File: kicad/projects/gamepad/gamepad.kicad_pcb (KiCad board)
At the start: 2 copper layers, 203.2 x 97.8 mm, 71 parts, among them J1 peripheral_addr_bus_connector, J10 Pad 2 SNES, J11 Conn_01x03_Pin, J2 peripheral_aux_connector, J3 peripheral_membank_connector, J4 PAD 1 ACTIVE, J5 PAD 2 ACTIVE, J6 Conn_02x05_Odd_Even, J7 Pad 1 header, J8 Pad 1 SNES, J9 Pad 2 header, U1 74HC161, U10 74HC245, U11 74HC245, U12 74HC245, U13 74HC245, U14 74HC00, U2 74HC161, U3 74HC595, U4 74HC595, U5 74HC595, U6 74HC595, U7 74HC14, U8 74HC00, U9 74HC161

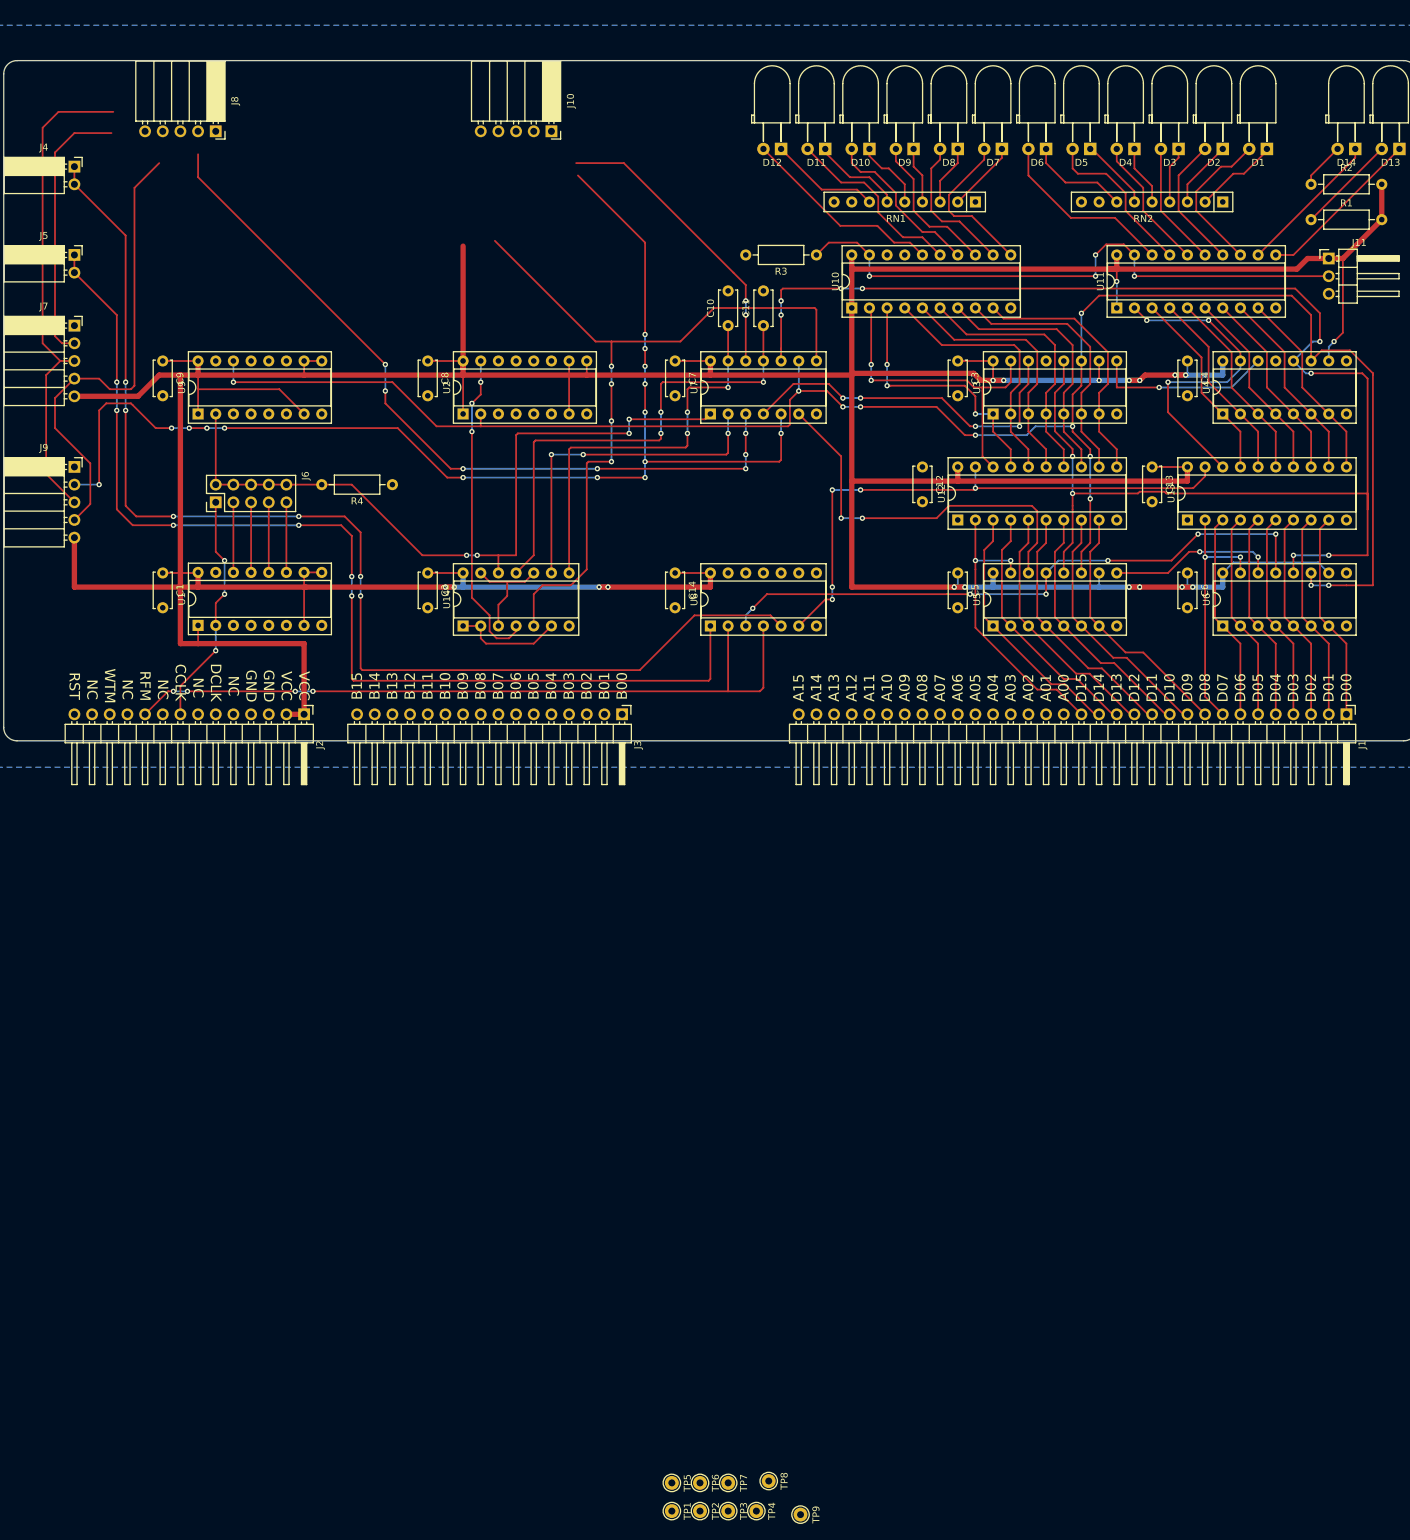
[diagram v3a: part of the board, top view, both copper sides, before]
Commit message: Add gamepad connector and almost complete on gamepad PCB
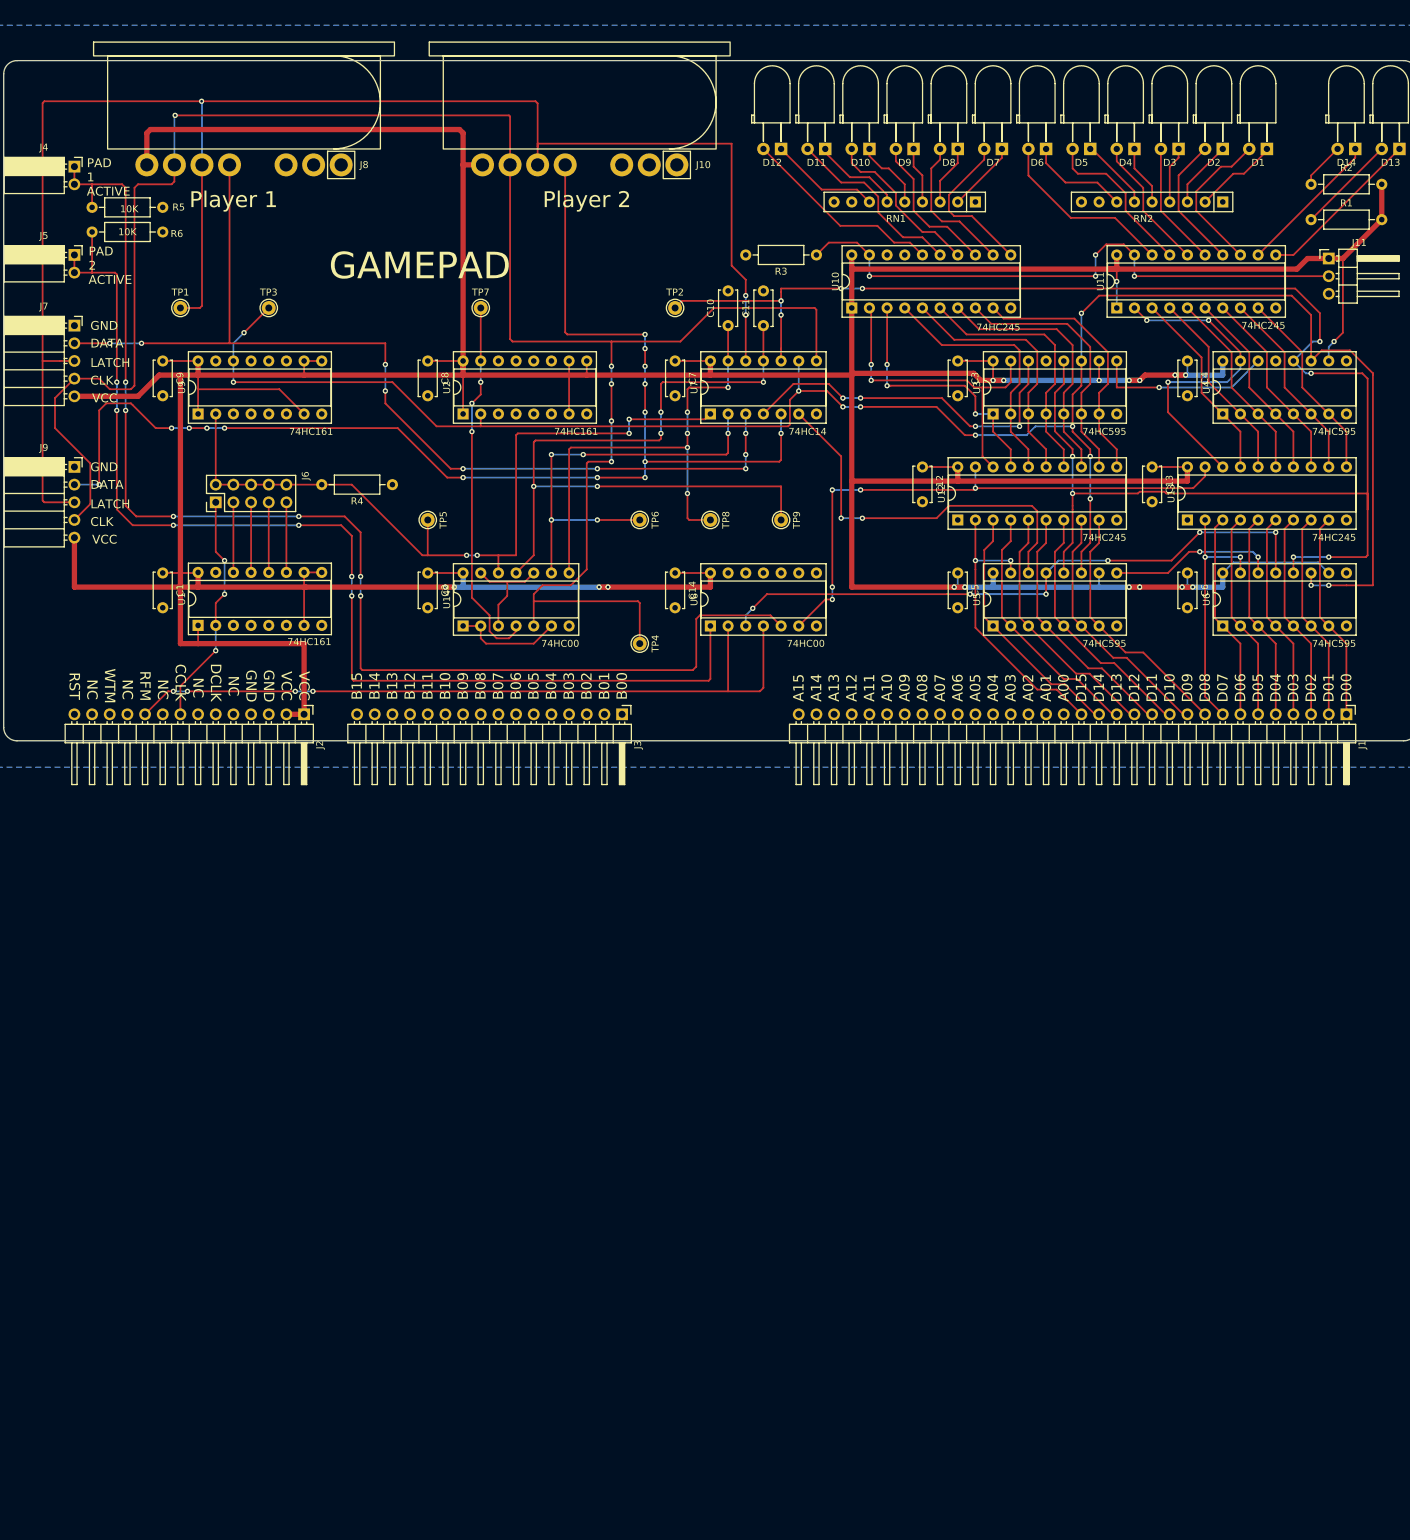
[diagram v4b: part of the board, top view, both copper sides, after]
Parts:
- added R5: 10K, Resistor_THT:R_Axial_DIN0207_L6.3mm_D2.5mm_P10.16mm_Horizontal, F.Cu at (63.5, 71.9)
- added R6: 10K, Resistor_THT:R_Axial_DIN0207_L6.3mm_D2.5mm_P10.16mm_Horizontal, F.Cu at (63.5, 75.4)
- J10, J8: footprint Connector_PinSocket_2.54mm:PinSocket_1x05_P2.54mm_Horizontal -> sixteen-bit-computer:snes-rightangle-connector
- moved TP1 186.8 mm to (76.2, 86.4), turned to 180 degrees
- moved TP3 185.2 mm to (88.9, 86.4), turned to 180 degrees
- moved TP2 173.0 mm to (147.3, 86.4), turned to 180 degrees
- moved TP7 172.6 mm to (119.4, 86.4), turned to 180 degrees
- moved TP9 143.0 mm to (162.6, 116.8)
- moved TP5 142.8 mm to (111.8, 116.8)
- moved TP6 138.7 mm to (142.2, 116.8)
- moved TP8 138.4 mm to (152.4, 116.8)
- moved TP4 125.8 mm to (142.2, 134.6)
- moved J10 18.7 mm to (147.6, 65.8), turned to 0 degrees
- moved J8 18.7 mm to (99.3, 65.8), turned to 0 degrees
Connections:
- J10 pad 2: /PAD 2 DATA -> unconnected-(J10-Pin_2-Pad2)
- J10 pad 3: /GAMEPAD LATCH -> unconnected-(J10-Pin_3-Pad3)
- J10 pad 4: /GAMEPAD CLK -> /PAD 2 DATA
- J10 pad 5: VCC -> /GAMEPAD LATCH
- J8 pad 2: /PAD 1 DATA -> unconnected-(J8-Pin_2-Pad2)
- J8 pad 3: /GAMEPAD LATCH -> unconnected-(J8-Pin_3-Pad3)
- J8 pad 4: /GAMEPAD CLK -> /PAD 1 DATA
- J8 pad 5: VCC -> /GAMEPAD LATCH
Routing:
- net /GAMEPAD LATCH: track 113.1 -> 239.7 mm, vias 2 -> 3
- net /GAMEPAD CLK: track 179.0 -> 283.0 mm, vias 4 -> 5
- net VCC: track 769.8 -> 844.4 mm
- net Net-(C11-Pad1): track 69.4 -> 109.8 mm, vias 3 -> 5
- net /SHIFT OUT REG CLK: track 226.1 -> 241.7 mm
- net Net-(C10-Pad1): track 58.0 -> 71.7 mm, vias 3 -> 5
- net /~{BASE CLK}: track 48.1 -> 60.8 mm, vias 3 -> 5
- net /PAD 1 ACTIVE: track 171.2 -> 182.5 mm
- net /PAD 2 ACTIVE: track 154.4 -> 164.2 mm
- net /SHIFT SERIAL CLK: track 273.3 -> 283.1 mm, vias 11 -> 12
- net /PAD 2 DATA: track 171.2 -> 180.1 mm
- net Net-(U2-TC): track 45.9 -> 53.5 mm
- net /PAD 1 DATA: track 149.5 -> 142.6 mm, vias 7 -> 9
- net /BASE CLK: track 107.8 -> 112.8 mm
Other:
- board text added: "CLK"
- board text added: "DATA"
- board text added: "GAMEPAD"
- board text added: "GND"
- board text added: "LATCH"
- board text added: "PAD 1 ACTIVE"
- board text added: "PAD 2 ACTIVE"
- board text added: "Player 1"
- board text added: "Player 2"
- board text added: "VCC"

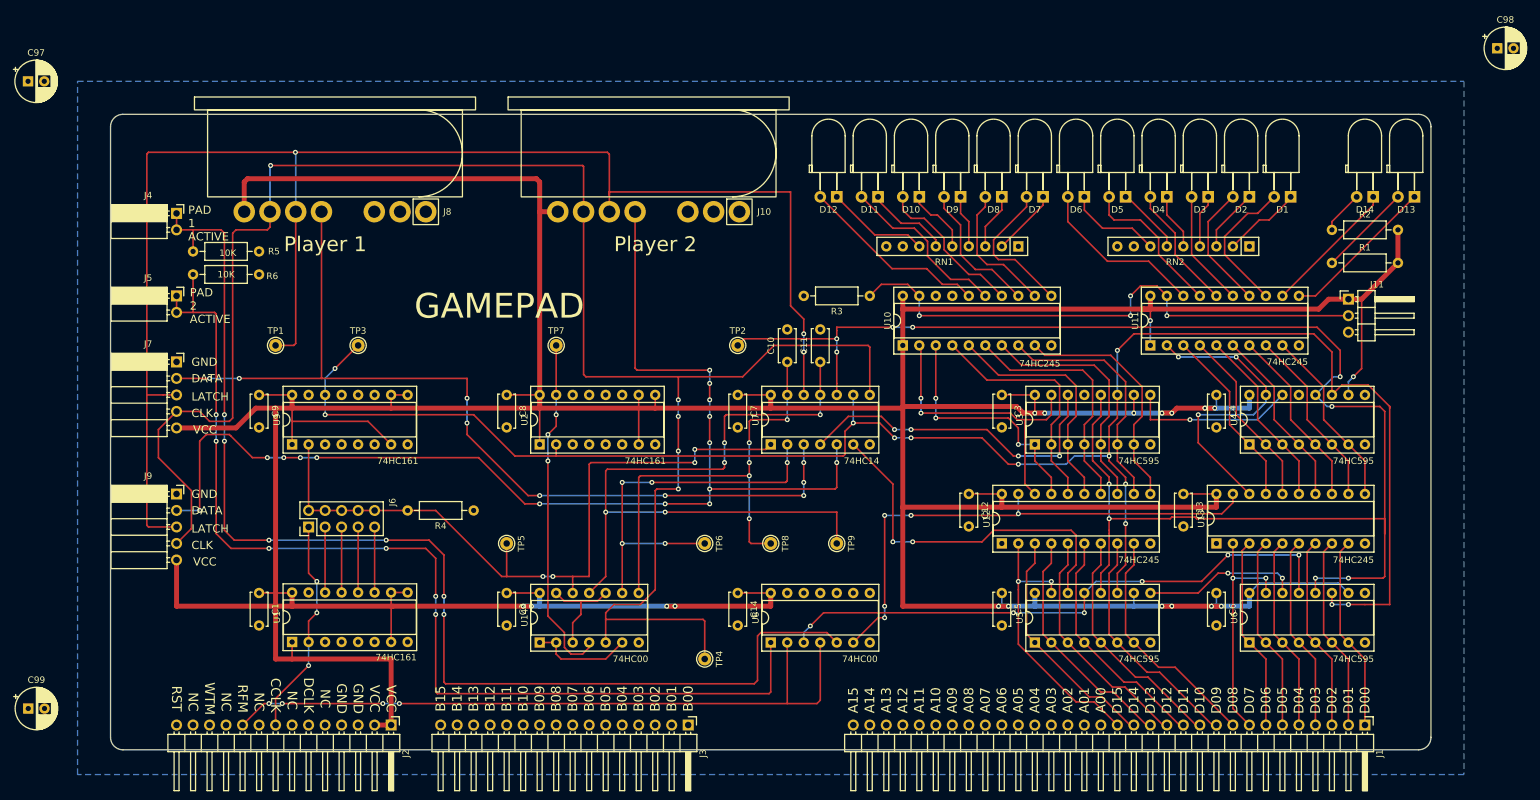
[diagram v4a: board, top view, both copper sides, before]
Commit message: Gamepad updated to single wie rfm wtm.
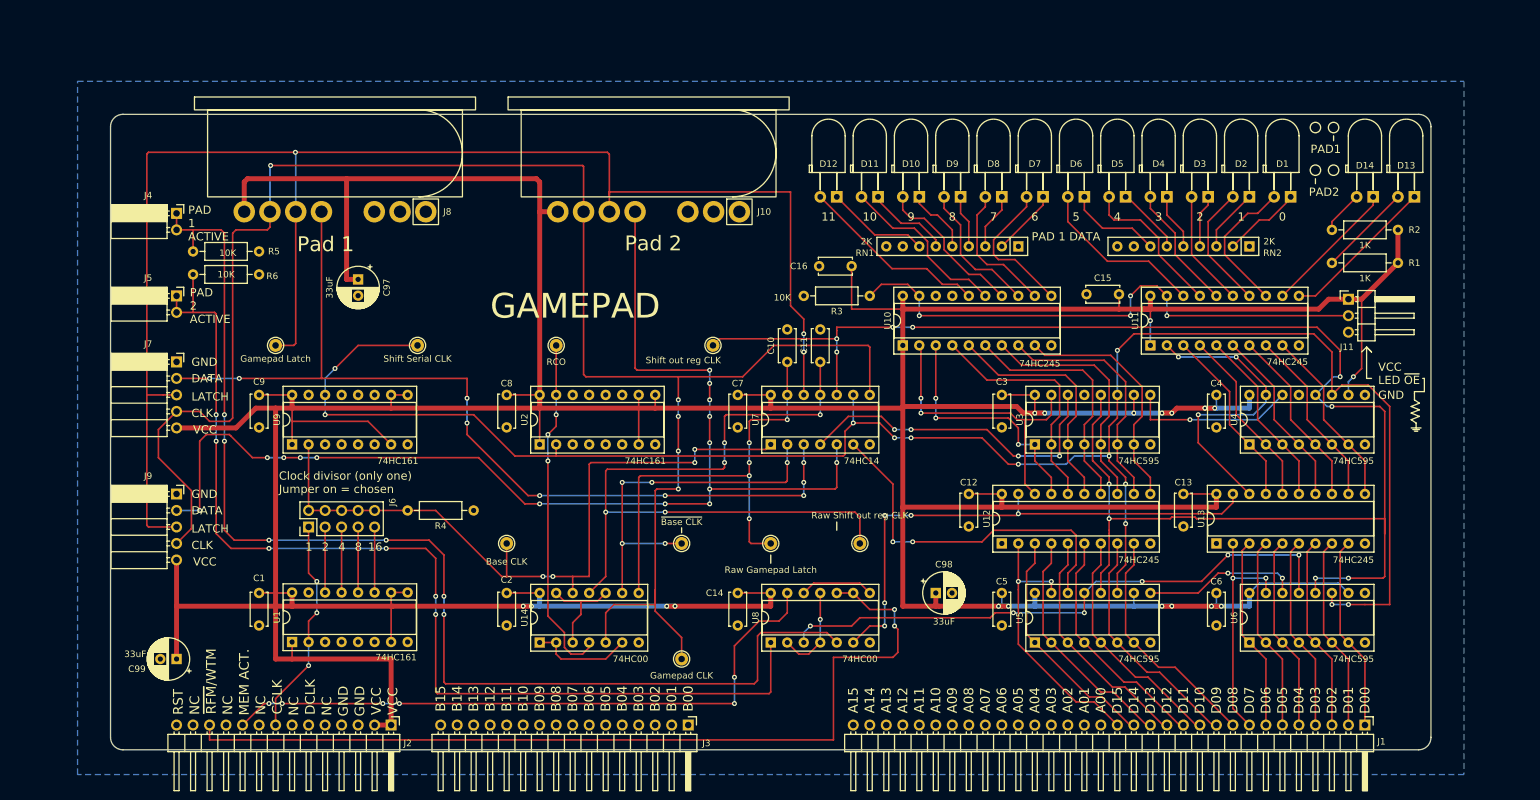
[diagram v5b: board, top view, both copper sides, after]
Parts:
- added C15: C, Capacitor_THT:C_Disc_D5.0mm_W2.5mm_P5.00mm, F.Cu at (201.0, 78.5)
- added C16: C, Capacitor_THT:C_Disc_D5.0mm_W2.5mm_P5.00mm, F.Cu at (159.8, 74.2)
- C97, C98, C99: value C_Polarized -> 33uF
- R1, R2: value R_US -> 1K
- RN1, RN2: value R_Network08_US -> 2K
- moved C98 120.4 mm to (177.8, 124.5)
- moved C97 59.2 mm to (88.9, 76.2), turned to -90 degrees
- moved C99 24.1 mm to (61.0, 134.6), turned to 180 degrees
- moved TP3 9.14 mm to (98.0, 86.4)
- moved TP2 3.81 mm to (143.5, 86.4)
- moved TP4 3.56 mm to (138.7, 134.6)
- moved TP6 3.56 mm to (138.7, 116.8)
- moved TP9 3.56 mm to (166.1, 116.8)
- turned J2 to 0 degrees
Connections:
- J2 pad 10: /RFM -> /MEM_ACTIVE
- J2 pad 12: /WTM -> /RFM_WTM
- U8 pad 10: GND -> /RFM_WTM
- U8 pad 11: unconnected-(U8-Pad11) -> /MEMACTIVE_RFM
- U8 pad 12: GND -> Net-(U8-Pad12)
- U8 pad 13: GND -> /MEM_ACTIVE
- U8 pad 2: /RFM -> /MEMACTIVE_RFM
- U8 pad 4: /RFM -> /MEMACTIVE_RFM
- U8 pad 8: unconnected-(U8-Pad8) -> Net-(U8-Pad12)
- U8 pad 9: GND -> /RFM_WTM
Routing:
- net /RFM_WTM: track 0.00 -> 138.0 mm, vias 0 -> 2
- net /RFM: track 108.8 -> 0.00 mm, vias 4 -> 0
- net /MEM_ACTIVE: track 0.00 -> 99.2 mm, vias 0 -> 6
- net VCC: track 844.4 -> 888.6 mm
- net /MEMACTIVE_RFM: track 0.00 -> 14.2 mm, vias 0 -> 1
- net Net-(U8-Pad12): track 0.00 -> 11.4 mm
- net /SHIFT SERIAL CLK: track 283.1 -> 291.9 mm
- net /GAMEPAD CLK: track 283.0 -> 275.5 mm
- net /SHIFT OUT REG CLK: track 241.7 -> 245.5 mm
- net /~{BASE CLK}: track 60.8 -> 57.3 mm
- net Net-(C11-Pad1): track 109.8 -> 112.7 mm
- net /PAD 1 ~{OE}: track 81.0 -> 81.7 mm
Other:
- board text added: "0"
- board text added: "1"
- board text added: "10"
- board text added: "11"
- board text added: "16"
- board text added: "2"
- board text added: "3"
- board text added: "4"
- board text added: "5"
- board text added: "6"
- board text added: "7"
- board text added: "8"
- board text added: "9"
- board text added: "Clock divisor (only one) Jumper on = chosen"
- board text added: "LED ~{OE}"
- board text added: "PAD 1 DATA"
- board text added: "PAD1"
- board text added: "PAD2"
- board text added: "Pad 1"
- board text added: "Pad 2"
- board text removed: "Player 1"
- board text removed: "Player 2"
